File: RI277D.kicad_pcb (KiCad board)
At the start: 2 copper layers, 240 x 100.3 mm, 72 parts, among them J1 Ribbon Cable, J2 SCN TRR TRT SCN - +

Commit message: version 1.2 prototype ready
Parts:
- removed the J1 at (234.9, 130.8)
- removed the J1 at (237.5, 82.5)
- removed the J1 at (196.8, 130.8)
- removed the J1 at (158.8, 130.8)
- removed the J1 at (161.3, 82.5)
- removed the J1 at (120.7, 130.8)
- removed the J1 at (72.4, 82.5)
- removed the J1 at (69.8, 130.8)
- removed the J1 at (31.8, 130.8)
- removed the J2 at (234.9, 149.9)
- removed the J2 at (256.5, 82.5)
- removed the J2 at (196.8, 149.9)
- removed the J2 at (158.8, 149.9)
- removed the J2 at (180.3, 82.5)
- removed the J2 at (120.7, 149.9)
- removed the J2 at (91.4, 82.5)
- removed the J2 at (69.8, 149.9)
- removed the J2 at (31.8, 149.9)
- removed the R2 at (214.6, 78.7)
- removed the R2 at (238.8, 108.0)
- removed the R2 at (200.7, 108.0)
- removed the R2 at (138.4, 78.7)
- removed the R2 at (162.6, 108.0)
- removed the R2 at (124.5, 108.0)
- removed the R2 at (49.5, 78.7)
- removed the R2 at (73.7, 108.0)
- removed the R2 at (35.6, 108.0)
- removed the R3 at (200.7, 82.5)
- removed the R3 at (234.9, 94.0)
- removed the R3 at (196.8, 94.0)
- removed the R3 at (124.5, 82.5)
- removed the R3 at (158.8, 94.0)
- removed the R3 at (120.7, 94.0)
- removed the R3 at (35.6, 82.5)
- removed the R3 at (69.8, 94.0)
- removed the R3 at (31.8, 94.0)
- removed the SK1 at (238.8, 134.6)
- removed the SK1 at (241.3, 78.7)
- removed the SK1 at (200.7, 134.6)
- removed the SK1 at (162.6, 134.6)
- removed the SK1 at (165.1, 78.7)
- removed the SK1 at (124.5, 134.6)
- removed the SK1 at (76.2, 78.7)
- removed the SK1 at (73.7, 134.6)
- removed the SK1 at (35.6, 134.6)
- removed the SK2 at (248.9, 133.3)
- removed the SK2 at (240.0, 68.6)
- removed the SK2 at (210.8, 133.3)
- removed the SK2 at (172.7, 133.3)
- removed the SK2 at (163.8, 68.6)
- removed the SK2 at (134.6, 133.3)
- removed the SK2 at (74.9, 68.6)
- removed the SK2 at (83.8, 133.3)
- removed the SK2 at (45.7, 133.3)
- removed the SK3 at (248.9, 113.0)
- removed the SK3 at (219.7, 68.6)
- removed the SK3 at (210.8, 113.0)
- removed the SK3 at (172.7, 113.0)
- removed the SK3 at (143.5, 68.6)
- removed the SK3 at (134.6, 113.0)
- removed the SK3 at (54.6, 68.6)
- removed the SK3 at (83.8, 113.0)
- removed the SK3 at (45.7, 113.0)
- removed the SK4 at (248.9, 92.7)
- removed the SK4 at (199.4, 68.6)
- removed the SK4 at (210.8, 92.7)
- removed the SK4 at (172.7, 92.7)
- removed the SK4 at (123.2, 68.6)
- removed the SK4 at (134.6, 92.7)
- removed the SK4 at (34.3, 68.6)
- removed the SK4 at (83.8, 92.7)
- removed the SK4 at (45.7, 92.7)
- added J1: Ribbon Cable, Connector_Molex:Molex_KK-254_AE-6410-10A_1x10_P2.54mm_Vertical, F.Cu at (69.8, 174.0)
- added J2: Tape Return, Connector_Molex:Molex_KK-254_AE-6410-03A_1x03_P2.54mm_Vertical, F.Cu at (87.6, 171.4)
- added R2: 1k, Resistor_THT:R_Axial_DIN0207_L6.3mm_D2.5mm_P10.16mm_Horizontal, F.Cu at (45.7, 168.9)
- added R3: 3k, Resistor_THT:R_Axial_DIN0207_L6.3mm_D2.5mm_P10.16mm_Horizontal, F.Cu at (32.4, 174.0)
- added SK1: MIC Input, Connector_Molex:Molex_KK-254_AE-6410-03A_1x03_P2.54mm_Vertical, F.Cu at (80.0, 171.4)
- added SK2: Line Input, Cliff:CL13345, F.Cu at (81.3, 146.1)
- added SK3: Insert, Cliff:CL13345, F.Cu at (61.0, 146.1)
- added SK4: Direct Out, Cliff:CL13345, F.Cu at (40.6, 146.1)
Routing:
- net (no net): track 3255.9 -> 0.00 mm, vias 16 -> 0
- net Net-(J2-Pad1): track 140.7 -> 0.00 mm, vias 2 -> 0
- net GND: track 0.00 -> 122.5 mm, vias 0 -> 2
- net Net-(J1-Pad1): track 10.2 -> 6.13 mm
- net Net-(J1-Pad2): track 18.8 -> 16.3 mm
- net Net-(R2-Pad2): track 27.3 -> 29.5 mm
- net Net-(J1-Pad8): track 32.8 -> 34.6 mm
- net Net-(J1-Pad6): track 55.6 -> 57.3 mm
- net Net-(J1-Pad4): track 18.2 -> 19.7 mm
- net Net-(J1-Pad5): track 31.5 -> 30.1 mm
- net Net-(J1-Pad10): track 30.6 -> 31.9 mm
- net Net-(J1-Pad9): track 27.7 -> 28.7 mm
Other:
- board size 240 x 100.3 mm -> 62 x 37 mm
- board text added: "R2"
- board text added: "R3"
- board text added: "SK1"
- board text added: "SK2"
- board text added: "SK3"
- board text added: "SK4"
- board text added: "v1.2"
- board text removed: "1"
- board text removed: "2"
- board text removed: "3"
- board text removed: "v1.1"

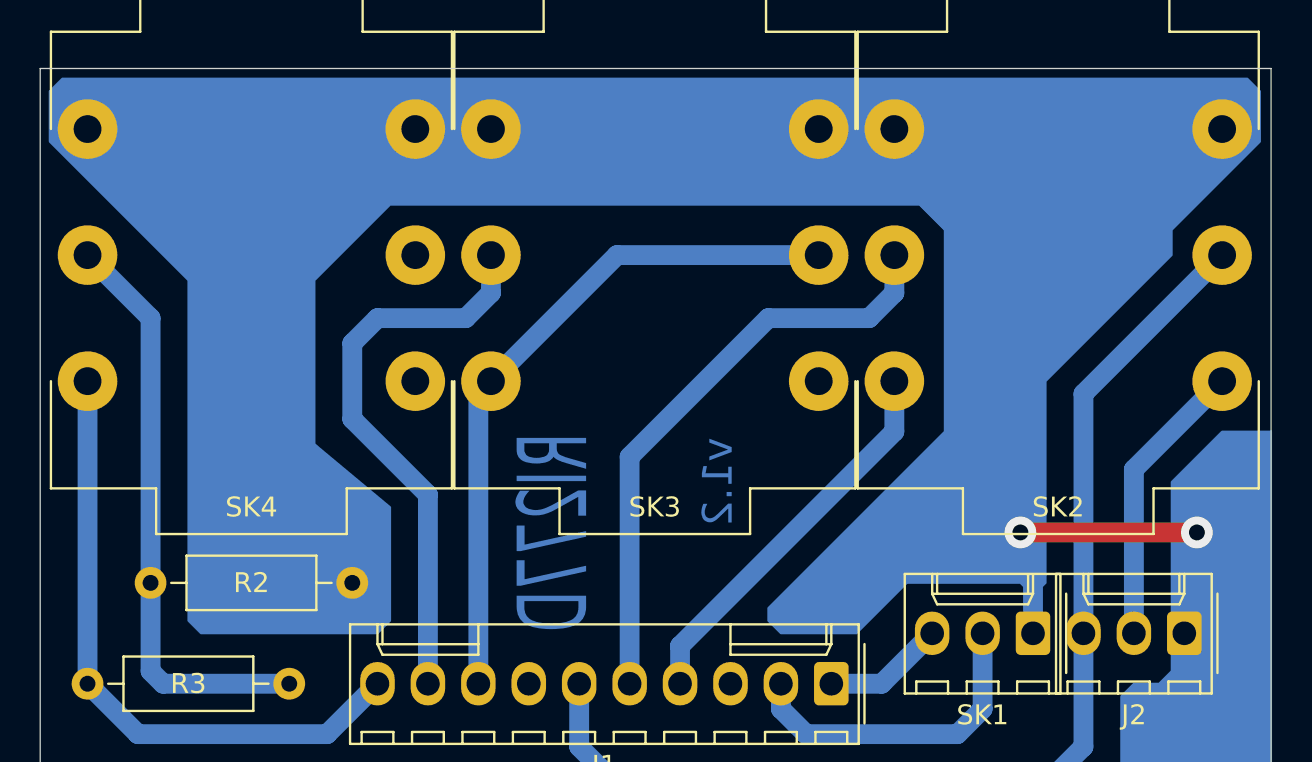
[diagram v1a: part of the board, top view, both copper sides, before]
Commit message: added git submodule library and wirebridge to layout
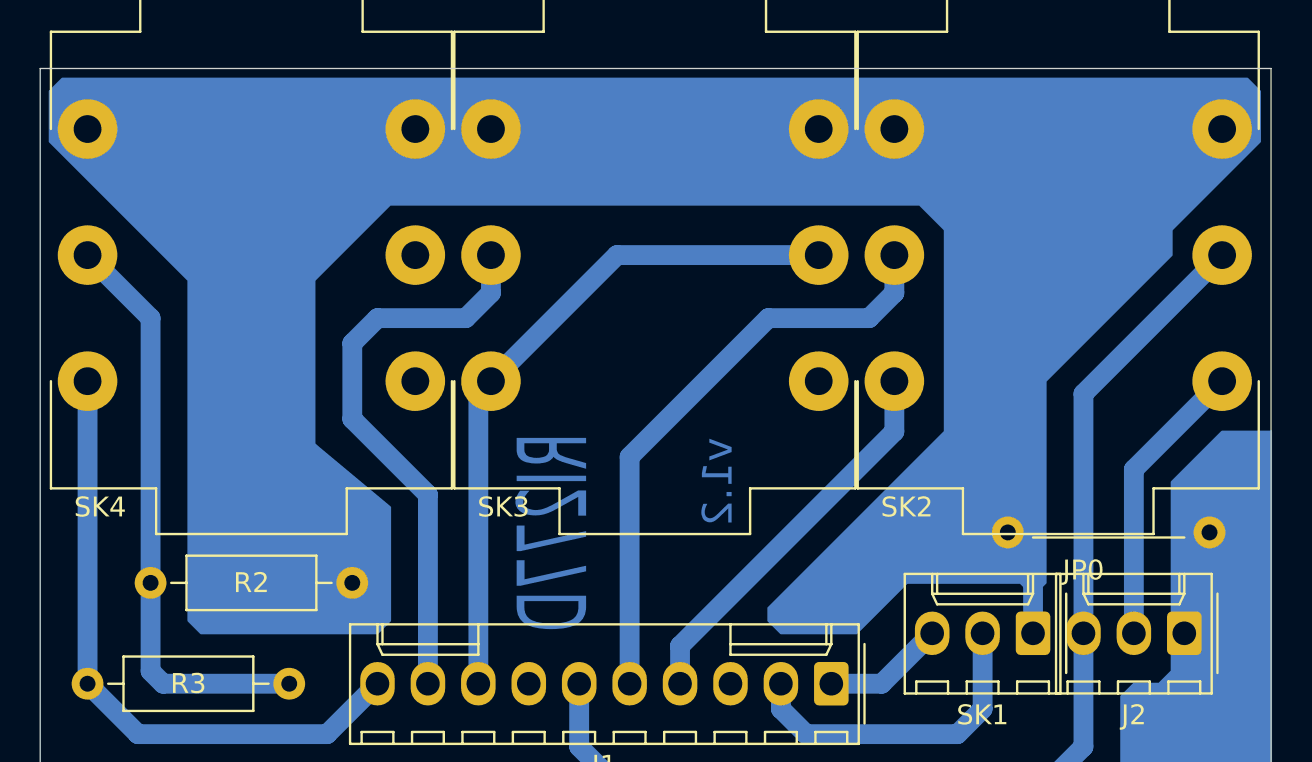
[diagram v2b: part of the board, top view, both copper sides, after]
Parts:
- added JP0: Wire_Bridge, TAC:Wire_Bridge_P10.16mm_Horizontal, F.Cu at (88.9, 166.4)
- SK2, SK3, SK4: footprint Cliff:CL13345 -> TAC:CL13345
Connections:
- J2 pad 1: GND -> Net-(J2-Pad1)
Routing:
- net GND: track 122.5 -> 107.3 mm, vias 2 -> 0
- net Net-(J2-Pad1): track 0.00 -> 5.61 mm
